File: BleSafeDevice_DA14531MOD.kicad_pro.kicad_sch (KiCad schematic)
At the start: 21 parts, among them J1 Conn_01x04, J2 EXT_PWR, SW1 1825910-6, U4 DA14531MOD-00F01002

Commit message: Reconcile button, power switch bypass, and bulk capacitor
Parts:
- C1: value 47uF 6.3V -> 100uF 6.3V
- S1: value MSK12C02 -> MSK12C02 (DNP - bypassed for prototype v1); now not fitted; now left out of the parts list
- SW1: value 1825910-6 -> PTS526SK15SMTR2 LFS; footprint 1825910-6:SW4_1825910-B_TEC -> SafeGuardPing_Local:SW_Push_1P1T_NO_CK_PTS526SK15SMTR2_LFS; symbol 2025-08-04_20-25-58:1825910-6 -> SafeGuardPing_Local:PTS526SK15SMTR2_LFS; MPN (none) -> PTS526SK15SMTR2 LFS
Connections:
- net VBAT: now also D2.1, S1.2
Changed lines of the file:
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@@
 	(wire
 		(pts
+			(xy 140.97 113.03) (xy 156.21 113.03)
+		)
+		(stroke
+			(width 0)
+			(type default)
+		)
+	)
+	(wire
+		(pts
+			(xy 156.21 113.03) (xy 156.21 115.57)
+		)
+		(stroke
+			(width 0)
+			(type default)
+		)
+	)
+	(wire
+		(pts
 			(xy 125.73 82.55) (xy 130.81 82.55)
 		)
@@
 		(unit 1)
 		(exclude_from_sim no)
-		(in_bom yes)
-		(on_board yes)
-		(dnp no)
+		(in_bom no)
+		(on_board no)
+		(dnp yes)
 		(fields_autoplaced yes)
 		(property "Reference" "S1"
@@
 			)
 		)
-		(property "Value" "MSK12C02"
+		(property "Value" "MSK12C02 (DNP - bypassed for prototype v1)"
 			(at 148.59 110.49 0)
 			(effects
@@
 	)
 	(symbol
-		(lib_id "2025-08-04_20-25-58:1825910-6")
+		(lib_id "SafeGuardPing_Local:PTS526SK15SMTR2_LFS")
 		(at 83.82 146.05 0)
 		(mirror y)
@@
 			)
 		)
-		(property "Value" "1825910-6"
+		(property "Value" "PTS526SK15SMTR2 LFS"
 			(at 63.5 138.43 0)
 			(effects
@@
 			)
 		)
-		(property "Footprint" "1825910-6:SW4_1825910-B_TEC"
+		(property "Footprint" "SafeGuardPing_Local:SW_Push_1P1T_NO_CK_PTS526SK15SMTR2_LFS"
 			(at 83.82 146.05 0)
 			(effects
@@
 			)
 		)
-		(property "Datasheet" "1825910-6"
+		(property "Datasheet" "https://www.littelfuse.com/assetdocs/littelfuse-ck-tactile-pts526-series-datasheet?assetguid=bb56c1b4-71ca-4262-9bd7-cf3e3c572bb3"
 			(at 83.82 146.05 0)
 			(effects
@@
 			)
 		)
-		(property "Description" ""
+		(property "Description" "C&K/Littelfuse PTS526 Series microminiature SMT top-actuated tactile switch, 1.5 mm height, 250 gf nominal, SPST-NO"
+			(at 83.82 146.05 0)
+			(effects
+				(font
+					(size 1.27 1.27)
+				)
+				(hide yes)
+			)
+		)
+		(property "MPN" "PTS526SK15SMTR2 LFS"
 			(at 83.82 146.05 0)
 			(effects
@@
 			)
 		)
-		(property "Value" "47uF 6.3V"
+		(property "Value" "100uF 6.3V"
 			(at 198.12 100.3299 90)
 			(effects

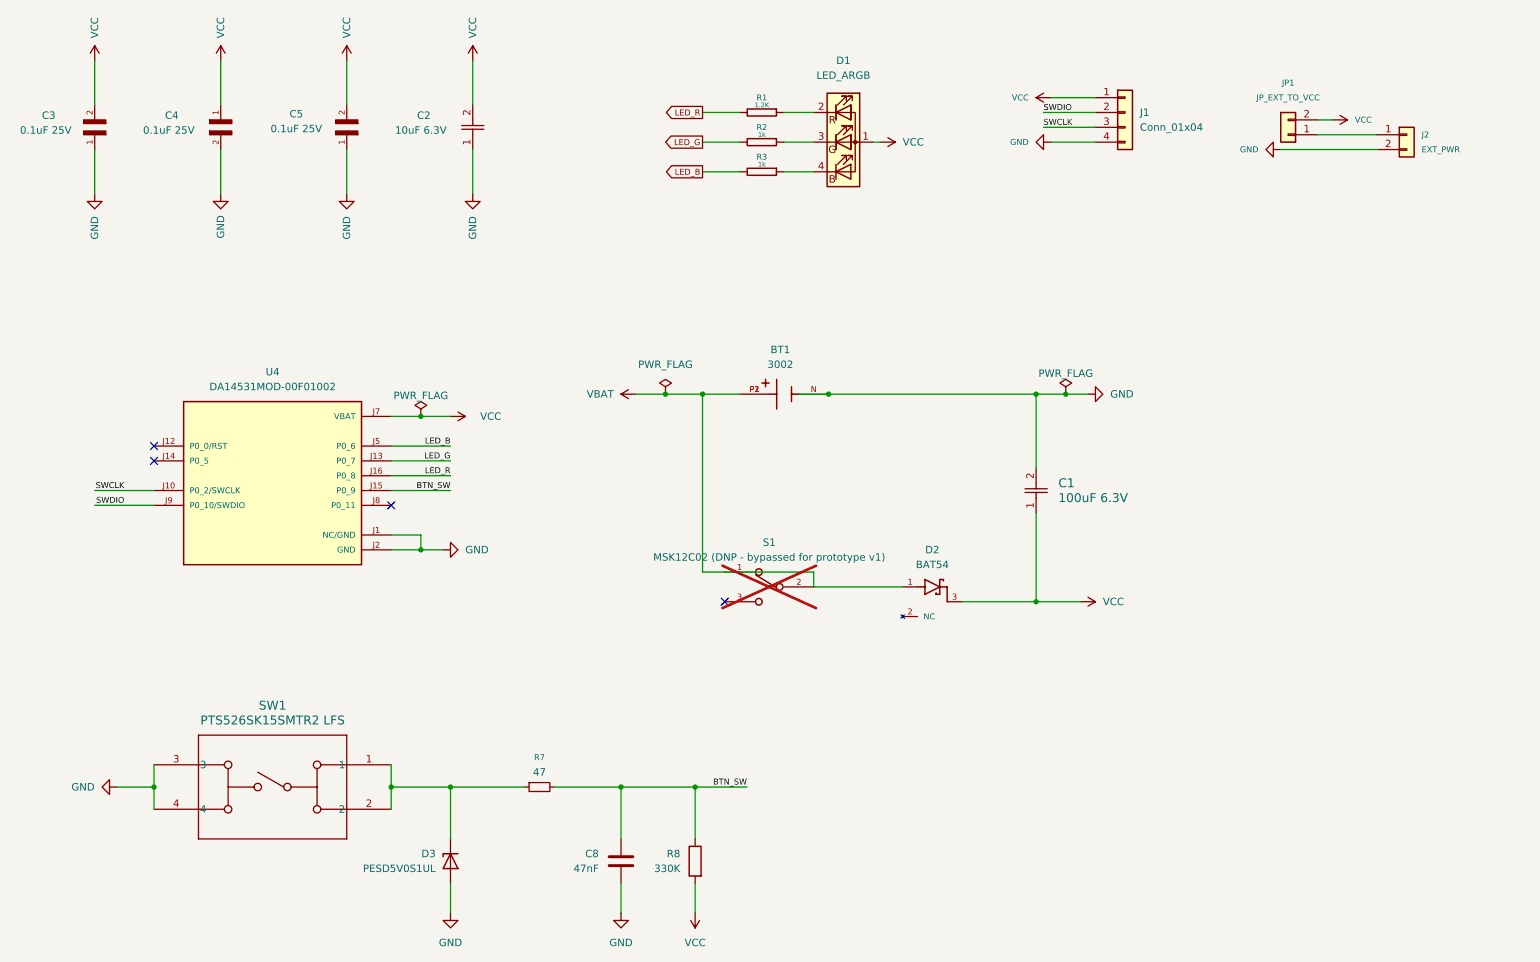
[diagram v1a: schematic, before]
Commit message: Simplify DA14531 reset and coin-cell power path
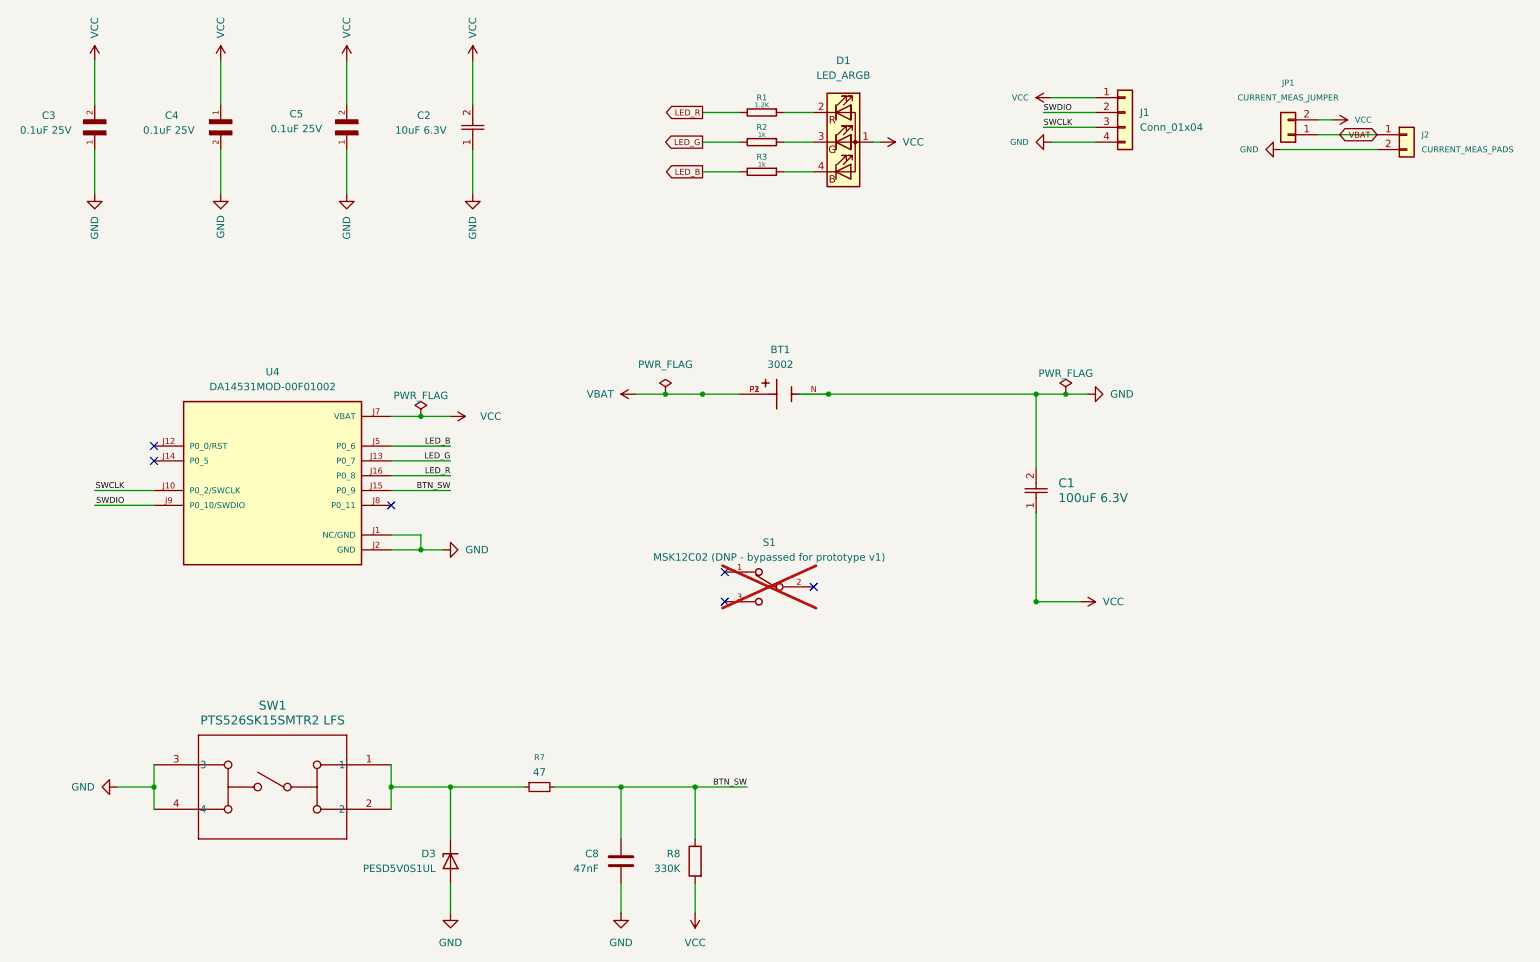
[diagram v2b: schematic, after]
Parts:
- removed D2: BAT54, myparts:SOT95P240X120-3N, symbol BAT54:BAT54
- J2: value EXT_PWR -> CURRENT_MEAS_PADS
- JP1: value JP_EXT_TO_VCC -> CURRENT_MEAS_JUMPER
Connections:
- net VBAT: now also J2.1 (Pin_1), JP1.1 (Pin_1); no longer S1.1, S1.2
- no-connect marks 4 -> 6

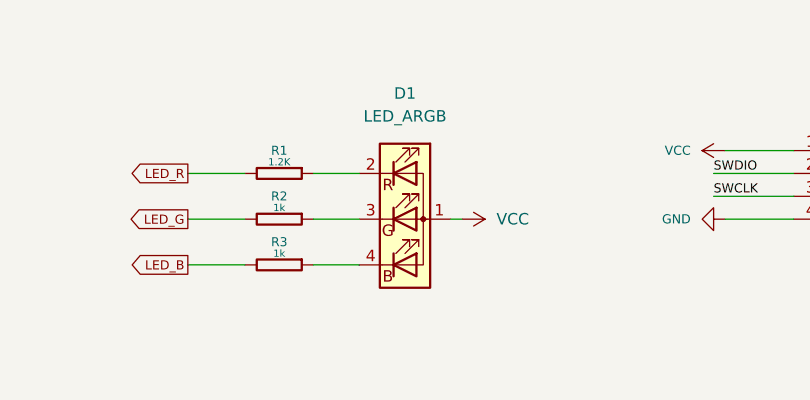
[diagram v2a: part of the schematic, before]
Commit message: Fix RGB LED footprint and metadata
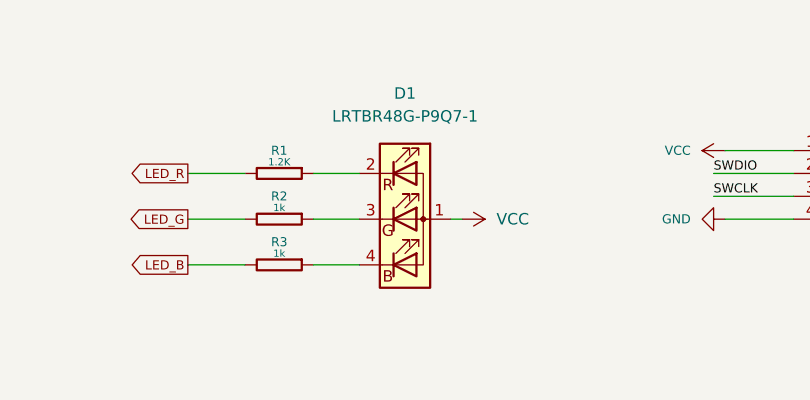
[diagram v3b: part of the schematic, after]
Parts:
- D1: value LED_ARGB -> LRTBR48G-P9Q7-1; footprint LED_SMD:LED_RGB_Wuerth-PLCC4_3.2x2.8mm_150141M173100 -> SafeGuardPing_Local:LED_RGB_amsOSRAM_LRTBR48G; MPN LRTBR48G-P9Q7-1 + R7S5-26 + NP-68-R33-ZB -> LRTBR48G-P9Q7-1+R7S5-26+NP-68
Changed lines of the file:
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@@
 			)
 		)
-		(property "Value" "LED_ARGB"
+		(property "Value" "LRTBR48G-P9Q7-1"
 			(at 161.29 27.94 0)
 			(effects
@@
 			)
 		)
-		(property "Footprint" "LED_SMD:LED_RGB_Wuerth-PLCC4_3.2x2.8mm_150141M173100"
+		(property "Footprint" "SafeGuardPing_Local:LED_RGB_amsOSRAM_LRTBR48G"
 			(at 161.29 40.64 0)
 			(effects
@@
 			)
 		)
-		(property "Datasheet" "~"
+		(property "Datasheet" "https://www.alldatasheet.com/datasheet-pdf/pdf/1047991/OSRAM/LRTB-R48G.html"
 			(at 161.29 40.64 0)
 			(effects
@@
 			)
 		)
-		(property "Description" "RGB LED, anode/red/green/blue"
+		(property "Description" "ams OSRAM LRTB R48G RGB LED, 1.0 mm x 1.0 mm, common anode; pin 1 A, pin 2 red K, pin 3 green K, pin 4 blue K"
 			(at 161.29 39.37 0)
 			(effects
@@
 			)
 		)
-		(property "MPN" "LRTBR48G-P9Q7-1 + R7S5-26 + NP-68-R33-ZB"
+		(property "MPN" "LRTBR48G-P9Q7-1+R7S5-26+NP-68"
 			(at 161.29 39.37 0)
 			(effects

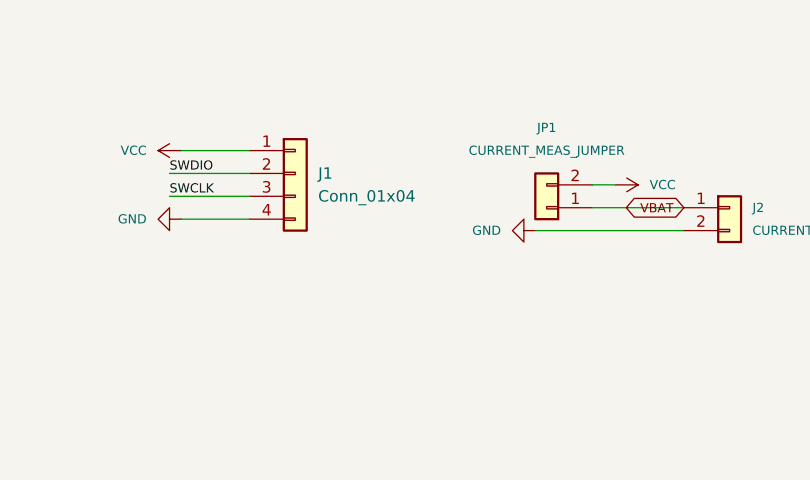
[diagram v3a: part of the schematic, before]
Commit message: Replace bulky debug and measurement headers with compact pads
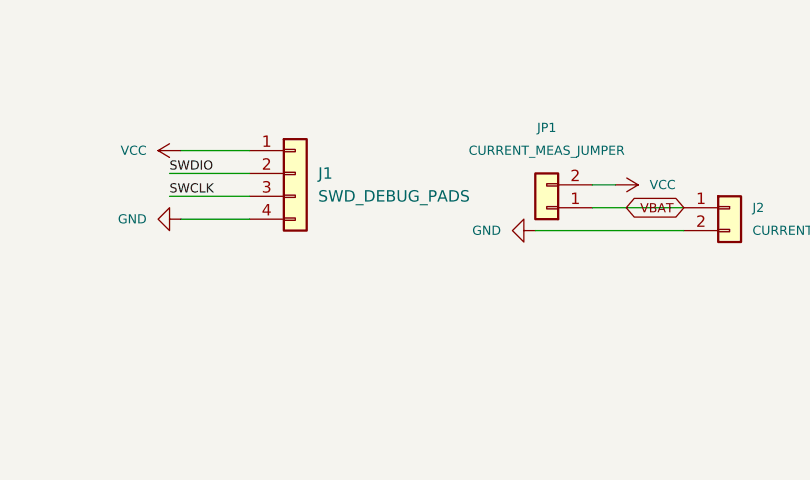
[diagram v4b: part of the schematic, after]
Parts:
- J1: value Conn_01x04 -> SWD_DEBUG_PADS; footprint Connector_PinHeader_2.54mm:PinHeader_1x04_P2.54mm_Vertical -> SafeGuardPing_Local:TP_SWD_1x04_1.27mm_Compact
- J2: footprint Connector_PinHeader_2.54mm:PinHeader_1x02_P2.54mm_Vertical -> SafeGuardPing_Local:TP_1x02_1.27mm_Compact
- JP1: footprint Connector_PinHeader_2.54mm:PinHeader_1x02_P2.54mm_Vertical -> SafeGuardPing_Local:TP_Current_Jumper_2Pad_Compact
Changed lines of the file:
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@@
 			)
 		)
-		(property "Footprint" "Connector_PinHeader_2.54mm:PinHeader_1x02_P2.54mm_Vertical"
+		(property "Footprint" "SafeGuardPing_Local:TP_1x02_1.27mm_Compact"
 			(at 257.81 38.1 0)
 			(effects
@@
 			)
 		)
-		(property "Footprint" "Connector_PinHeader_2.54mm:PinHeader_1x02_P2.54mm_Vertical"
+		(property "Footprint" "SafeGuardPing_Local:TP_Current_Jumper_2Pad_Compact"
 			(at 237.49 38.1 0)
 			(effects
@@
 			)
 		)
-		(property "Value" "Conn_01x04"
+		(property "Value" "SWD_DEBUG_PADS"
 			(at 212.09 36.8299 0)
 			(effects
@@
 			)
 		)
-		(property "Footprint" "Connector_PinHeader_2.54mm:PinHeader_1x04_P2.54mm_Vertical"
+		(property "Footprint" "SafeGuardPing_Local:TP_SWD_1x04_1.27mm_Compact"
 			(at 209.55 34.29 0)
 			(effects

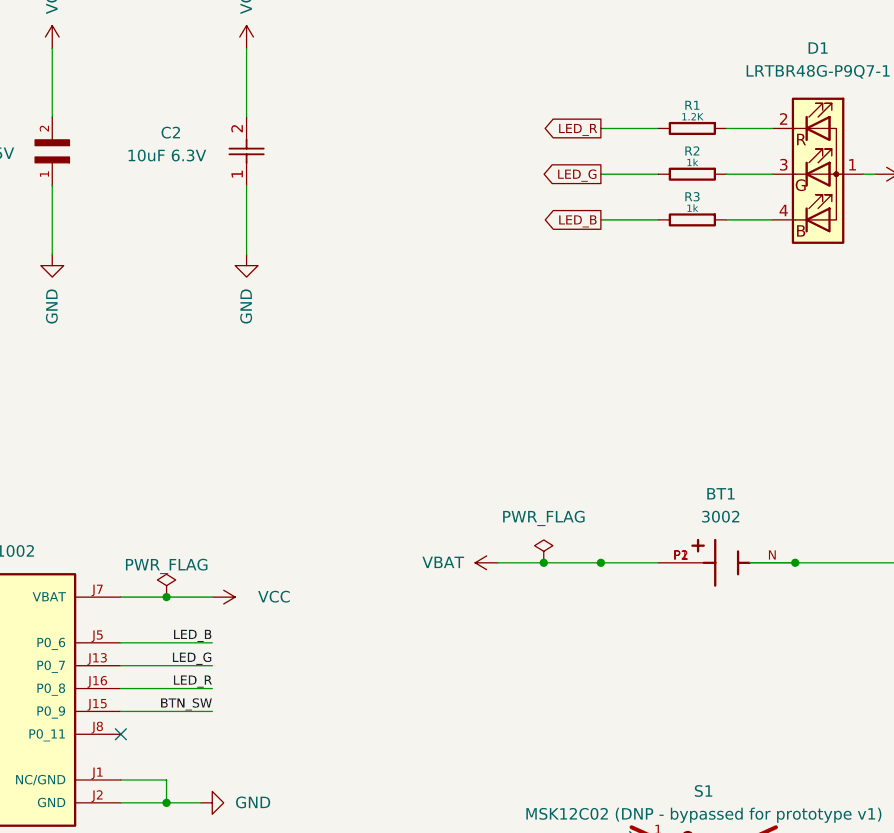
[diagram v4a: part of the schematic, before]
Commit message: Simplify LED to red status channel and complete routing
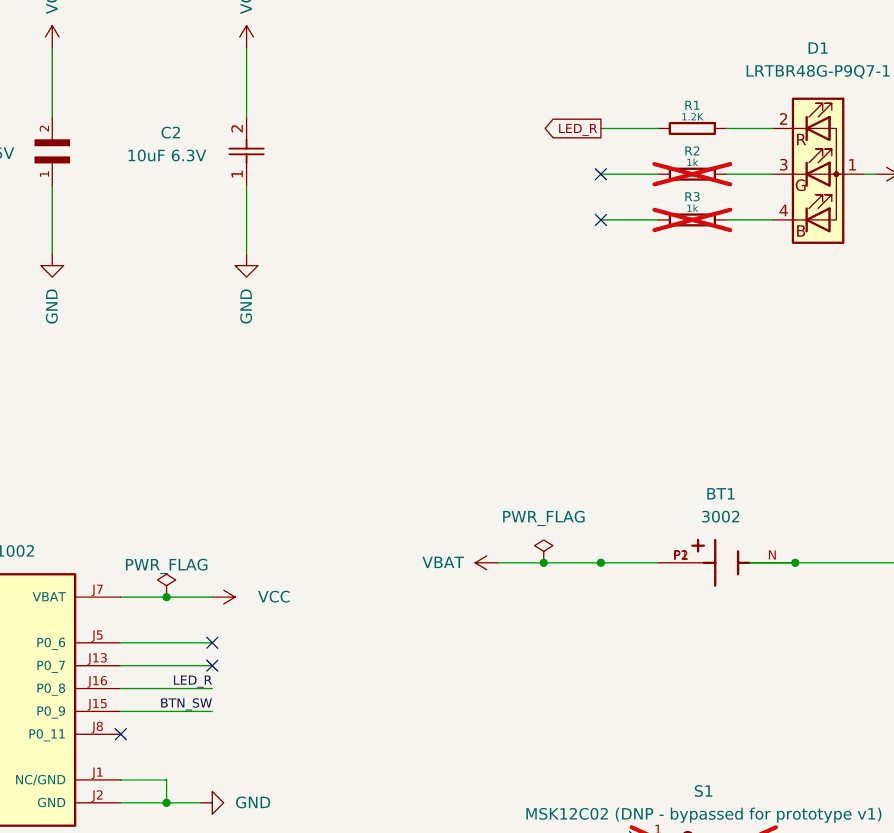
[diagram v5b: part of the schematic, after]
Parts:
- R2, R3: now not fitted; now left out of the parts list
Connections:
- net LED_B: no longer names the net of U4.J5 (P0_6)
- net LED_B: no longer R3.2
- net LED_G: no longer names the net of U4.J13 (P0_7)
- net LED_G: no longer R2.2
- no-connect marks 6 -> 10
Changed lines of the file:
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@@
 		(at 83.82 101.6)
+	)
+	(no_connect
+		(at 93.98 91.44)
+	)
+	(no_connect
+		(at 93.98 93.98)
+	)
+	(no_connect
+		(at 137.16 39.37)
+	)
+	(no_connect
+		(at 137.16 44.45)
 	)
 	(wire
@@
 		)
 	)
-	(label "LED_B"
-		(at 93.98 91.44 180)
-		(effects
-			(font
-				(size 1.016 1.016)
-			)
-			(justify right bottom)
-		)
-	)
 	(label "LED_R"
 		(at 93.98 96.52 180)
-		(effects
-			(font
-				(size 1.016 1.016)
-			)
-			(justify right bottom)
-		)
-	)
-	(label "LED_G"
-		(at 93.98 93.98 180)
 		(effects
 			(font
@@
 		(property "Intersheetrefs" "${INTERSHEET_REFS}"
 			(at 245.7943 38.1 0)
-			(effects
-				(font
-					(size 1.27 1.27)
-				)
-				(justify right)
-				(hide yes)
-			)
-		)
-	)
-	(global_label "LED_G"
-		(shape output)
-		(at 137.16 39.37 180)
-		(fields_autoplaced yes)
-		(effects
-			(font
-				(size 1.016 1.016)
-			)
-			(justify right)
-		)
-		(property "Intersheetrefs" "${INTERSHEET_REFS}"
-			(at 130.2243 39.37 0)
-			(effects
-				(font
-					(size 1.27 1.27)
-				)
-				(justify right)
-				(hide yes)
-			)
-		)
-	)
-	(global_label "LED_B"
-		(shape output)
-		(at 137.16 44.45 180)
-		(fields_autoplaced yes)
-		(effects
-			(font
-				(size 1.016 1.016)
-			)
-			(justify right)
-		)
-		(property "Intersheetrefs" "${INTERSHEET_REFS}"
-			(at 130.2243 44.45 0)
 			(effects
 				(font
@@
 		(unit 1)
 		(exclude_from_sim no)
-		(in_bom yes)
-		(on_board yes)
-		(dnp no)
+		(in_bom no)
+		(on_board no)
+		(dnp yes)
 		(fields_autoplaced yes)
 		(property "Reference" "R3"
@@
 		(unit 1)
 		(exclude_from_sim no)
-		(in_bom yes)
-		(on_board yes)
-		(dnp no)
+		(in_bom no)
+		(on_board no)
+		(dnp yes)
 		(fields_autoplaced yes)
 		(property "Reference" "R2"

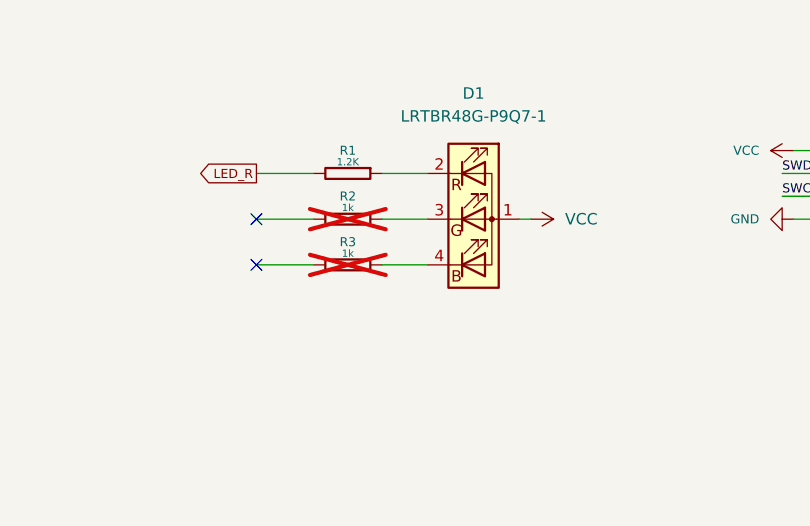
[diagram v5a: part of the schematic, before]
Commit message: Fix schematic PCB parity for prototype LED simplification
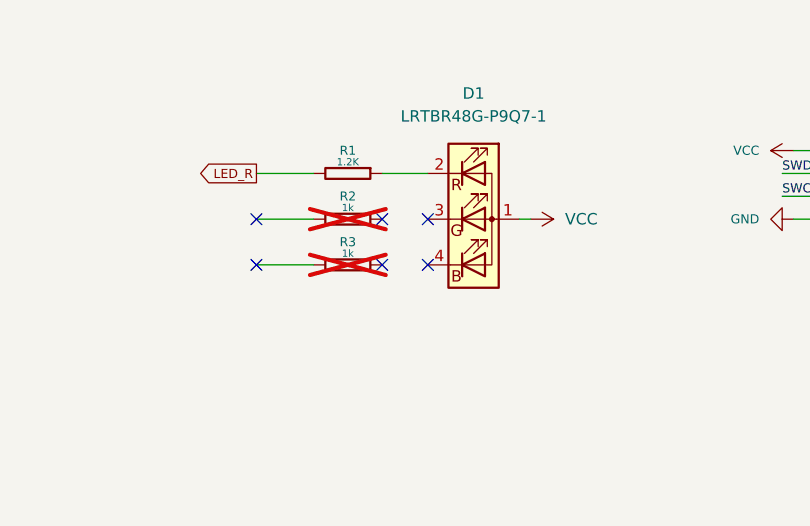
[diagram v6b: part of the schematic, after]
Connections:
- net at R3.1: no longer D1.4 (BK)
- net at R2.1: no longer D1.3 (GK)
- no-connect marks 10 -> 14
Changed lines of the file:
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@@
 		(at 137.16 44.45)
 	)
+	(no_connect
+		(at 156.21 39.37)
+	)
+	(no_connect
+		(at 156.21 44.45)
+	)
+	(no_connect
+		(at 151.13 39.37)
+	)
+	(no_connect
+		(at 151.13 44.45)
+	)
 	(wire
 		(pts
@@
 	(wire
 		(pts
-			(xy 151.13 44.45) (xy 156.21 44.45)
-		)
-		(stroke
-			(width 0)
-			(type default)
-		)
-	)
-	(wire
-		(pts
 			(xy 33.02 33.02) (xy 33.02 25.4)
 		)
@@
 		)
 		(stroke
-			(width 0)
-			(type default)
-		)
-	)
-	(wire
-		(pts
-			(xy 151.13 39.37) (xy 156.21 39.37)
-		)
-		(stroke
